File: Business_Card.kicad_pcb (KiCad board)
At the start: 2 copper layers, 85 x 55 mm, 1 part

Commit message: updated schematic
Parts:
- removed REF**: Coin_Battery_Holder_CR2032, Coin_Battery_Holder_CR2032:Coin_Battery_Holder_CR2032
- added BT1: Battery_Cell, Coin_Battery_Holder_CR2032:Coin_Battery_Holder_CR2032, F.Cu at (118.2, 75.8)
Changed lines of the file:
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@@
 	)
 	(net 0 "")
+	(net 1 "+3V0")
+	(net 2 "GND")
 	(footprint "Coin_Battery_Holder_CR2032:Coin_Battery_Holder_CR2032"
 		(layer "F.Cu")
-		(at 120 76)
-		(property "Reference" "REF**"
+		(at 118.25 75.75)
+		(property "Reference" "BT1"
 			(at 18 -10.5 0)
 			(unlocked yes)
@@
 			)
 		)
-		(property "Value" "Coin_Battery_Holder_CR2032"
-			(at 11 -23 0)
+		(property "Value" "Battery_Cell"
+			(at 11.25 -22.5 0)
 			(unlocked yes)
 			(layer "F.Fab")
@@
 			)
 		)
-		(property "Datasheet" ""
+		(property "Datasheet" "~"
 			(at 0 0 0)
 			(unlocked yes)
@@
 			)
 		)
-		(property "Description" ""
+		(property "Description" "Single-cell battery"
 			(at 0 0 0)
 			(unlocked yes)
@@
 			)
 		)
+		(sheetname "/")
+		(sheetfile "Business_Card.kicad_sch")
 		(attr through_hole)
 		(fp_line
@@
 			(chamfer_ratio 0.25)
 			(chamfer top_left top_right bottom_left bottom_right)
+			(net 1 "+3V0")
+			(pinfunction "+")
+			(pintype "passive")
 		)
 		(pad "2" smd roundrect
@@
 			(chamfer_ratio 0.25)
 			(chamfer top_left top_right bottom_left bottom_right)
+			(net 2 "GND")
+			(pinfunction "-")
+			(pintype "passive")
 		)
 		(pad "2" smd roundrect
@@
 			(chamfer_ratio 0.25)
 			(chamfer top_left top_right bottom_left bottom_right)
+			(net 2 "GND")
+			(pinfunction "-")
+			(pintype "passive")
 		)
 		(embedded_fonts no)

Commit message: extra stuff
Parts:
- added BZ1: Buzzer, BUSINESS_CARD:piezo_buzzer, F.Cu at (86.4, 80.0)
- added C1: 10uF, BUSINESS_CARD:C_106, F.Cu at (109.8, 68.9)
- added C2: 0.1uF, BUSINESS_CARD:C_104, F.Cu at (54.3, 79.0)
- added J2: Conn_01x06, BUSINESS_CARD:conn_01x06, F.Cu at (68.4, 101.2)
- added LED1: RED_LED, BUSINESS_CARD:SMD_RED_LTST-S270KRKT, F.Cu at (58.2, 72.8)
- added LED2: GREEN_LED, BUSINESS_CARD:SMD__GREEN_LTST-C170GKT_LTO, F.Cu at (59.0, 67.8)
- added LED3: YELLOW_LED, BUSINESS_CARD:YELLOW_LED_.LTST-C190KSKT, F.Cu at (52.8, 69.8)
- added LED4: WON_LED, BUSINESS_CARD:SMD_RED_LTST-S270KRKT, F.Cu at (131.7, 99.0)
- added LED5: LOST_LED, BUSINESS_CARD:SMD_RED_LTST-S270KRKT, F.Cu at (140.2, 99.0)
- added R1: 220Ω, BUSINESS_CARD:R_0221, F.Cu at (40.2, 55.1)
- added R2: 220Ω, BUSINESS_CARD:R_0221, F.Cu at (40.2, 60.0)
- added R3: 220Ω, BUSINESS_CARD:R_0221, F.Cu at (40.2, 65.0)
- added R4: 10k, BUSINESS_CARD:R_0103, F.Cu at (49.9, 79.4)
- added R5: 10k, BUSINESS_CARD:R_0103, F.Cu at (51.9, 79.4)
- added R6: 4.7k, BUSINESS_CARD:R_0472, F.Cu at (37.5, 78.6)
- added R7: 2.2k, BUSINESS_CARD:R_0222, F.Cu at (46.7, 76.5)
- added R8: 220Ω, BUSINESS_CARD:R_0221, F.Cu at (40.2, 70.0)
- added R9: 220, BUSINESS_CARD:R_0221, F.Cu at (40.2, 74.9)
- added RESET1: B3SN-3012P, BUSINESS_CARD:SW_B3SN-3012P, F.Cu at (137.0, 86.0)
- added SW1: B3SN-3012P, BUSINESS_CARD:SW_B3SN-3012P, F.Cu at (92.0, 97.0)
- added SW2: B3SN-3012P, BUSINESS_CARD:SW_B3SN-3012P, F.Cu at (105.0, 97.0)
- added SW3: B3SN-3012P, BUSINESS_CARD:SW_B3SN-3012P, F.Cu at (117.0, 97.0)
- added U1: ATtiny85-20M, Package_DFN_QFN:QFN-20-1EP_4x4mm_P0.5mm_EP2.6x2.6mm, F.Cu at (71.7, 92.3)

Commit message: Finished PCB
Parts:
- added G***: LOGO, LOGO, F.Cu at (69.7, 66.8)
- added G***: LOGO, LOGO, F.Cu at (69.7, 62.4)
- added G***: LOGO, LOGO, F.Cu at (69.7, 71.1)
- added G***: LOGO, LOGO, B.Cu at (90.7, 71.2)
- R1, R2, R3, R8, R9: footprint BUSINESS_CARD:R_0221 -> BUSINESS_CARD:221_R_RESC1005X40N
- YOU LOST: renamed from LED5
- YOU WON: renamed from LED4
- moved R8 104.6 mm to (142.1, 93.4), turned to -90 degrees
- moved R7 79.9 mm to (122.7, 101.2), turned to 90 degrees
- moved R6 76.1 mm to (110.2, 100.9), turned to 90 degrees
- moved LED3 66.2 mm to (116.4, 87.8), turned to 180 degrees
- moved R3 66.0 mm to (103.3, 84.3)
- moved R2 61.3 mm to (96.5, 84.3)
- moved R1 57.8 mm to (87.8, 87.8)
- moved R5 50.3 mm to (97.4, 100.6), turned to 180 degrees
- moved LED2 49.7 mm to (104.4, 87.9)
- moved LED1 36.9 mm to (91.9, 87.8)
- moved C2 33.8 mm to (84.7, 93.8), turned to -90 degrees
- moved R4 33.0 mm to (80.7, 91.2), turned to 90 degrees
- moved R9 31.0 mm to (67.2, 90.1), turned to 180 degrees
- moved YOU WON 16.6 mm to (129.7, 82.5), turned to 180 degrees
- moved YOU LOST 16.5 mm to (140.3, 82.5)
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- renumbered RESET1 to RESET
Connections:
- J2 pad 5: +3V0 -> unconnected-(J2-Pin_5-Pad5)
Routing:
- net +3V0: track 0.00 -> 116.7 mm, vias 0 -> 3
- net /PB3: track 0.00 -> 102.0 mm, vias 0 -> 2
- net /RESET: track 0.00 -> 76.6 mm, vias 0 -> 6
- net Net-(LED1-K): track 0.00 -> 61.4 mm
- net /PB1: track 0.00 -> 53.0 mm, vias 0 -> 2
- net Net-(LED2-A): track 0.00 -> 52.8 mm
- net /PB2: track 0.00 -> 49.3 mm, vias 0 -> 2
- net Net-(LED1-A): track 0.00 -> 48.9 mm, vias 0 -> 2
- net /PB0: track 0.00 -> 30.7 mm, vias 0 -> 2
- net /PB4: track 0.00 -> 19.5 mm
- net Net-(R8-Pad2): track 0.00 -> 12.0 mm
- net Net-(R7-Pad2): track 0.00 -> 10.5 mm
- net Net-(R5-Pad2): track 0.00 -> 10.4 mm
- net Net-(R6-Pad2): track 0.00 -> 10.0 mm
- added copper zone on B.Cu, net GND
- added copper zone on F.Cu, net GND
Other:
- board text added: "+1 (111) 111-1111"
- board text added: "Electrical Engineering Student"
- board text added: "Jorge De Los Santos Razo"
- board text added: "JorgeDeLosRazo"
- board text added: "john.doe@gmail.com"
- board text removed: "Name :)"
- board text removed: "Phone Number"
- board text removed: "Profession"
- board text removed: "e-mail"

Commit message: cleared all the DRC errors
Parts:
- LED4: renamed from YOU WON
- LED5: renamed from YOU LOST
- moved C1 37.9 mm to (77.6, 91.9)
- moved R9 0.95 mm to (67.5, 89.2), turned to 90 degrees
- renumbered RESET to RESET1
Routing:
- net +3V0: track 116.7 -> 114.8 mm, vias 3 -> 2
- net /RESET: track 76.6 -> 77.1 mm
- net GND: vias 0 -> 4

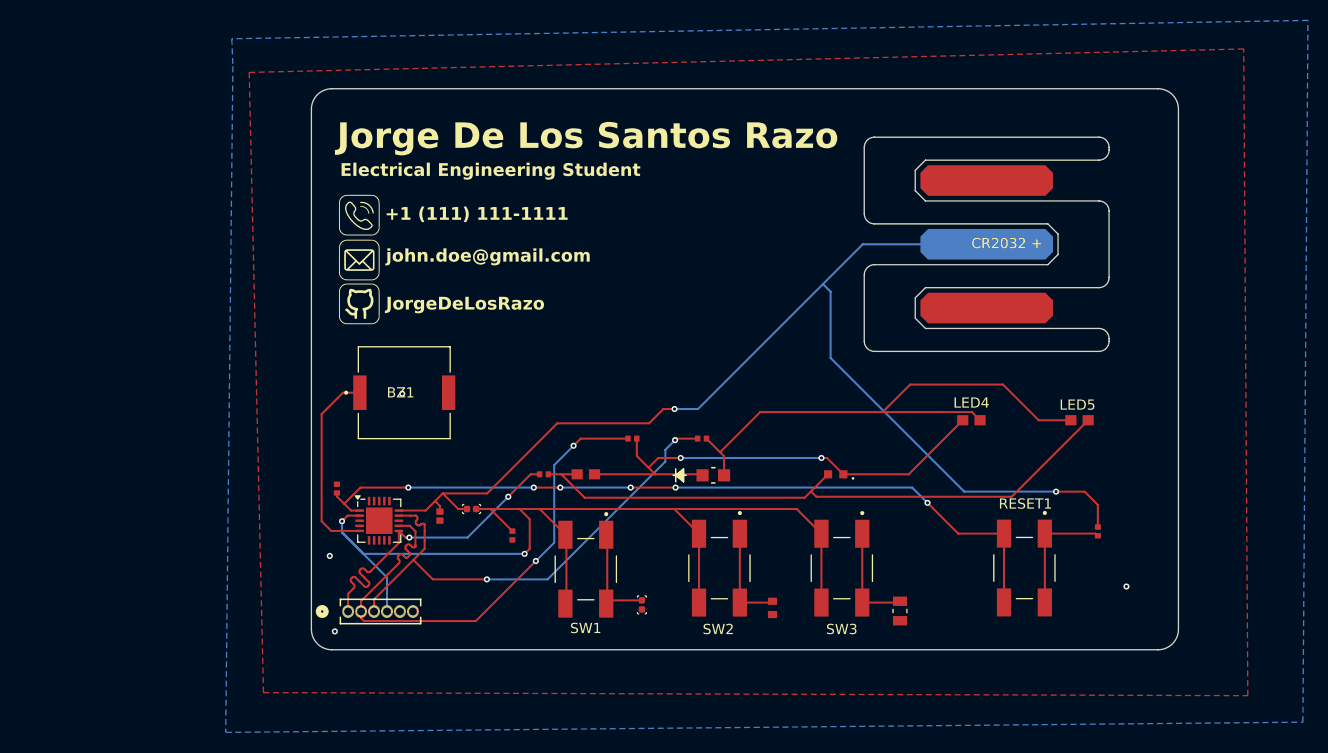
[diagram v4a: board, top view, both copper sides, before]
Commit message: created symbol folder
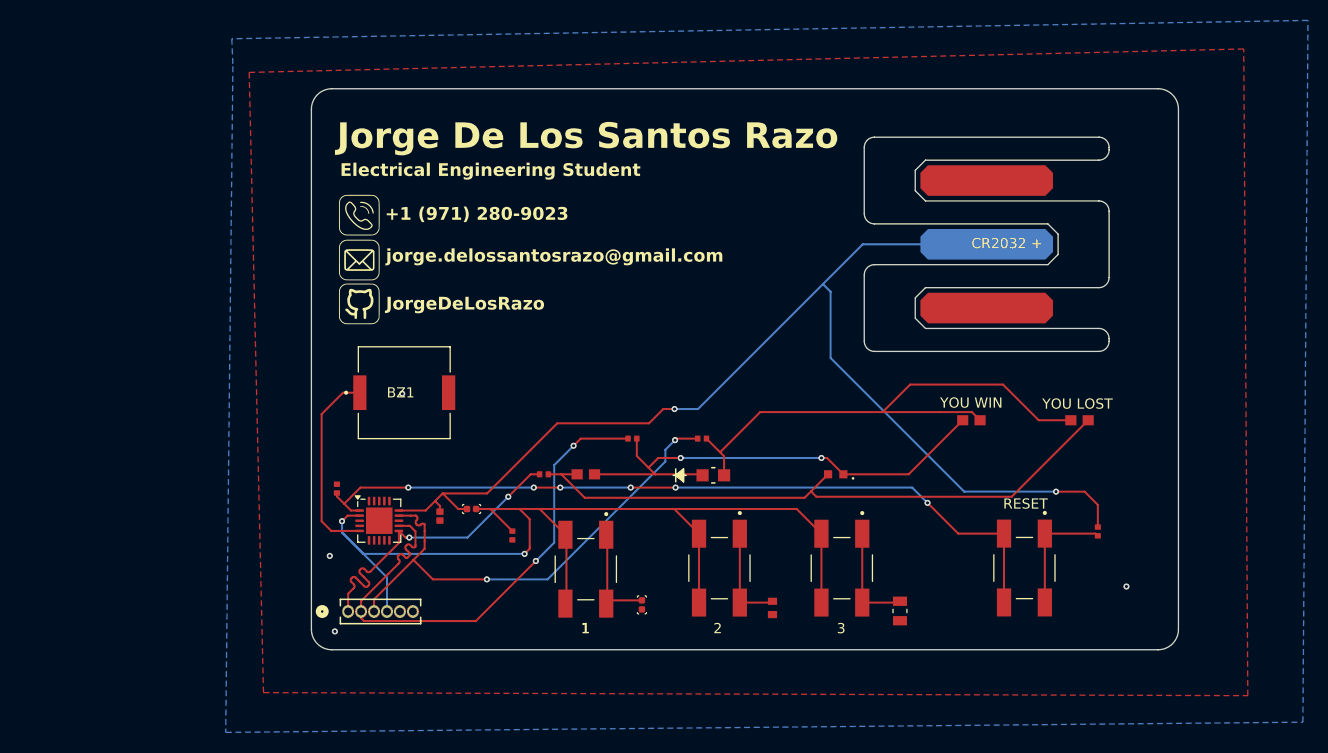
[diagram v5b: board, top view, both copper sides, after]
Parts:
- renumbered SW1 to 1, SW2 to 2, SW3 to 3, RESET1 to RESET
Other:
- board text added: "+1 (971) 280-9023"
- board text added: "1"
- board text added: "2"
- board text added: "3"
- board text added: "YOU LOST"
- board text added: "YOU WIN"
- board text added: "jorge.delossantosrazo@gmail.com"
- board text removed: "+1 (111) 111-1111"
- board text removed: "john.doe@gmail.com"
